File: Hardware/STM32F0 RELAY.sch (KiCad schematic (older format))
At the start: 22 parts, among them Q2 Q_NMOS_GSD, U10 STM32F030RCT6, Y3 32.768kHz, Y4 8MHz

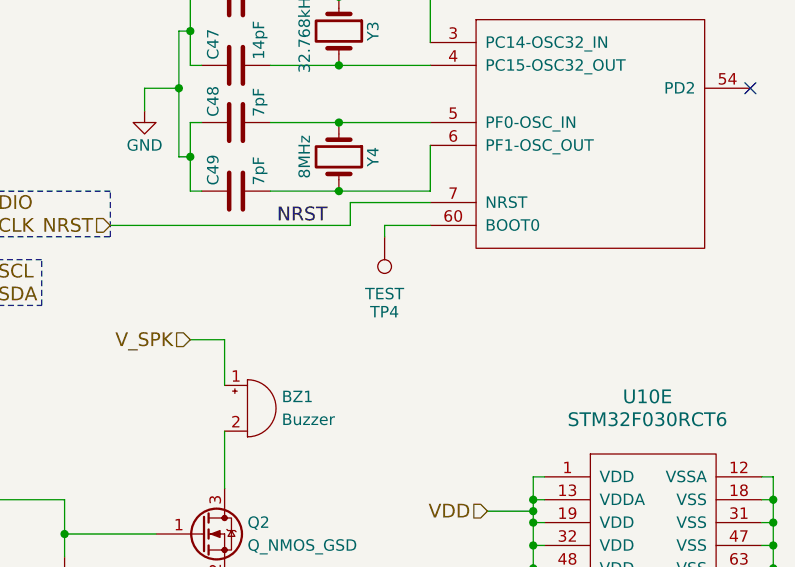
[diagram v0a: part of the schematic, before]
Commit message: Bug fixes, added Isense, changed conn to JST-GH
Added boot0 pull-down resistors. Changed ext_batt to current sense line. Changed spox conn to JST-GH, this will dramatically reduce the required size of the board.
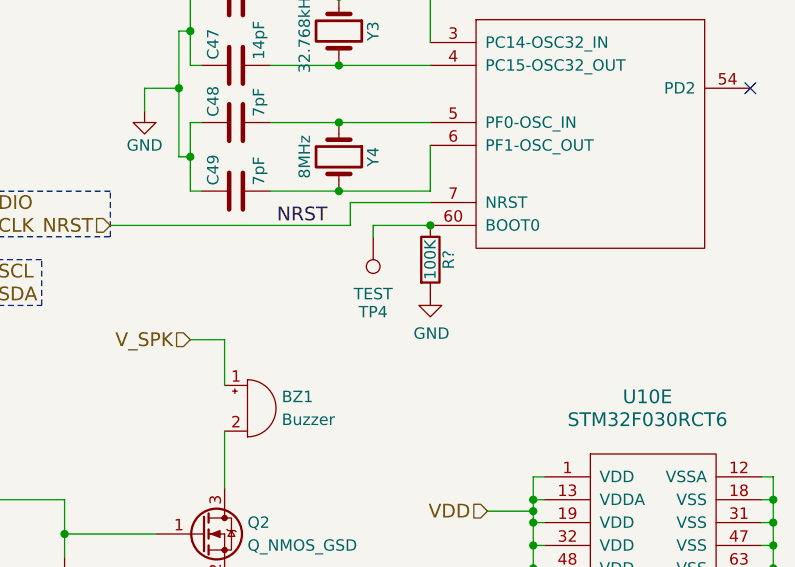
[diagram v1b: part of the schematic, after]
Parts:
- added R?: 100K, Resistors_SMD:R_0603_HandSoldering, symbol Device:R
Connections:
- net GND: now also R?.2
- net at TP4.1, U10.60 (BOOT0): now also R?.1
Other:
- moved on the sheet: TP4
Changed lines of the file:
@@
 L Connector:TestPoint TP4
 U 1 1 596A3495
-P 7200 3200
-F 0 "TP4" H 7200 3500 50  0000 C BNN
-F 1 "TEST" H 7200 3450 50  0000 C CNN
-F 2 "Measurement_Points:Measurement_Point_Round-SMD-Pad_Small" H 7200 3200 50  0001 C CNN
-F 3 "" H 7200 3200 50  0001 C CNN
-	1    7200 3200
+P 7150 3200
+F 0 "TP4" H 7150 3500 50  0000 C BNN
+F 1 "TEST" H 7150 3450 50  0000 C CNN
+F 2 "Measurement_Points:Measurement_Point_Round-SMD-Pad_Small" H 7150 3200 50  0001 C CNN
+F 3 "" H 7150 3200 50  0001 C CNN
+	1    7150 3200
 	-1   0    0    1
 $EndComp
 Wire Wire Line
-	7200 3200 7200 3150
-Wire Wire Line
-	7200 3150 7400 3150
+	7150 3200 7150 3150
+Wire Wire Line
+	7150 3150 7400 3150
 NoConn ~ 3900 5400
 NoConn ~ 3900 5300
@@
 Wire Notes Line
 	3050 2900 3050 2700
+$Comp
+L Device:R R?
+U 1 1 5CBCEAA5
+P 7400 3300
+F 0 "R?" V 7480 3300 50  0000 C CNN
+F 1 "100K" V 7400 3300 50  0000 C CNN
+F 2 "Resistors_SMD:R_0603_HandSoldering" V 7330 3300 50  0001 C CNN
+F 3 "http://www.yageo.com/documents/recent/PYu-RC_Group_51_RoHS_L_10.pdf" H 7400 3300 50  0001 C CNN
+F 4 "RESS-008" V 7400 3300 60  0001 C CNN "part_num"
+	1    7400 3300
+	1    0    0    -1
+$EndComp
+Connection ~ 7400 3150
 Wire Bus Line
 	1400 3700 1400 5350
+$Comp
+L power:GND #PWR?
+U 1 1 5CBD6D08
+P 7400 3450
+F 0 "#PWR?" H 7400 3200 50  0001 C CNN
+F 1 "GND" H 7405 3277 50  0000 C CNN
+F 2 "" H 7400 3450 50  0001 C CNN
+F 3 "" H 7400 3450 50  0001 C CNN
+	1    7400 3450
+	1    0    0    -1
+$EndComp
 $EndSCHEMATC

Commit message: Added protection diode to USB
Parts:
- R?: value 100K -> 10K; part_num RESS-008 -> RESS-005
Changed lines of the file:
@@
 P 7400 3300
 F 0 "R?" V 7480 3300 50  0000 C CNN
-F 1 "100K" V 7400 3300 50  0000 C CNN
+F 1 "10K" V 7400 3300 50  0000 C CNN
 F 2 "Resistors_SMD:R_0603_HandSoldering" V 7330 3300 50  0001 C CNN
 F 3 "http://www.yageo.com/documents/recent/PYu-RC_Group_51_RoHS_L_10.pdf" H 7400 3300 50  0001 C CNN
-F 4 "RESS-008" V 7400 3300 60  0001 C CNN "part_num"
+F 4 "RESS-005" V 7400 3300 60  0001 C CNN "part_num"
 	1    7400 3300
 	1    0    0    -1
 $EndComp
 Connection ~ 7400 3150
-Wire Bus Line
-	1400 3700 1400 5350
 $Comp
 L power:GND #PWR?
@@
 	1    0    0    -1
 $EndComp
+Wire Bus Line
+	1400 3700 1400 5350
 $EndSCHEMATC

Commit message: Removed F0 SPI, gave Baro its own I2C line, changed IMU to SPI1
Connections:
- net MISO: no longer names the net of U10.56 (PB4)
- net MOSI: no longer names the net of U10.57 (PB5)
- net NSS: no longer names the net of U10.50 (PA15)
- net SCLK: no longer names the net of U10.55 (PB3)
- no-connect marks 17 -> 21
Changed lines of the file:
@@
 EESchema Schematic File Version 4
-LIBS:ZeroPilot-cache
 EELAYER 26 0
 EELAYER END
@@
 Wire Wire Line
 	4950 5300 6150 5300
-Text HLabel 3200 4350 0    60   Input ~ 0
-MOSI
-Text HLabel 3200 4250 0    60   Input ~ 0
-MISO
-Text HLabel 4950 3250 2    60   Input ~ 0
-NSS
-Wire Wire Line
-	4950 3250 4850 3250
-Wire Wire Line
-	3900 4250 3200 4250
-Wire Wire Line
-	3200 4350 3900 4350
-Text HLabel 3200 4150 0    60   Input ~ 0
-SCLK
-Wire Wire Line
-	3200 4150 3900 4150
 $Comp
 L power:GND #PWR034
@@
 	1    0    0    -1
 $EndComp
+NoConn ~ 3900 4350
+NoConn ~ 3900 4250
+NoConn ~ 3900 4150
+NoConn ~ 4850 3250
 Wire Bus Line
 	1400 3700 1400 5350

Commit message: Generated netlist and board outline
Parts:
- gave numbers to parts that had none: 1
- renumbered D9 to D10, D7 to D8, D8 to D9, R20 to R23, R21 to R24, R22 to R25, R23 to R26, TP4 to TP7
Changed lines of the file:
@@
 Connection ~ 7200 5300
 $Comp
-L power:GND #PWR029
+L power:GND #PWR036
 U 1 1 59199AA1
 P 7450 5300
-F 0 "#PWR029" H 7450 5050 50  0001 C CNN
+F 0 "#PWR036" H 7450 5050 50  0001 C CNN
 F 1 "GND" H 7450 5150 50  0000 C CNN
 F 2 "" H 7450 5300 50  0001 C CNN
@@
 Connection ~ 6350 2300
 $Comp
-L power:GND #PWR030
+L power:GND #PWR032
 U 1 1 5919B18A
 P 6150 2650
-F 0 "#PWR030" H 6150 2400 50  0001 C CNN
+F 0 "#PWR032" H 6150 2400 50  0001 C CNN
 F 1 "GND" H 6150 2500 50  0000 C CNN
 F 2 "" H 6150 2650 50  0001 C CNN
@@
 	2500 4400 3200 4400
 $Comp
-L Device:LED D8
+L Device:LED D9
 U 1 1 59531E55
 P 5800 5750
-F 0 "D8" H 5800 5850 50  0000 C CNN
+F 0 "D9" H 5800 5850 50  0000 C CNN
 F 1 "LED" H 5800 5650 50  0000 C CNN
 F 2 "LEDs:LED_0603" H 5800 5750 50  0001 C CNN
@@
 $EndComp
 $Comp
-L Device:R R22
+L Device:R R25
 U 1 1 59531EA2
 P 5800 6150
-F 0 "R22" V 5880 6150 50  0000 C CNN
+F 0 "R25" V 5880 6150 50  0000 C CNN
 F 1 "100" V 5800 6150 50  0000 C CNN
 F 2 "Resistors_SMD:R_0603_HandSoldering" V 5730 6150 50  0001 C CNN
@@
 VDD
 $Comp
-L Connector:TestPoint TP4
+L Connector:TestPoint TP7
 U 1 1 596A3495
 P 7150 3200
-F 0 "TP4" H 7150 3500 50  0000 C BNN
+F 0 "TP7" H 7150 3500 50  0000 C BNN
 F 1 "TEST" H 7150 3450 50  0000 C CNN
 F 2 "Measurement_Points:Measurement_Point_Round-SMD-Pad_Small" H 7150 3200 50  0001 C CNN
@@
 NoConn ~ 4900 4250
 $Comp
-L Device:LED D7
+L Device:LED D8
 U 1 1 592CEFDB
 P 5450 5750
-F 0 "D7" H 5450 5850 50  0000 C CNN
+F 0 "D8" H 5450 5850 50  0000 C CNN
 F 1 "LED" H 5450 5650 50  0000 C CNN
 F 2 "LEDs:LED_0603" H 5450 5750 50  0001 C CNN
@@
 $EndComp
 $Comp
-L Device:R R20
+L Device:R R23
 U 1 1 592CEFE3
 P 5450 6150
-F 0 "R20" V 5530 6150 50  0000 C CNN
+F 0 "R23" V 5530 6150 50  0000 C CNN
 F 1 "100" V 5450 6150 50  0000 C CNN
 F 2 "Resistors_SMD:R_0603_HandSoldering" V 5380 6150 50  0001 C CNN
@@
 $EndComp
 $Comp
-L power:GND #PWR032
+L power:GND #PWR029
 U 1 1 592CEFEA
 P 5450 6400
-F 0 "#PWR032" H 5450 6150 50  0001 C CNN
+F 0 "#PWR029" H 5450 6150 50  0001 C CNN
 F 1 "GND" H 5450 6250 50  0000 C CNN
 F 2 "" H 5450 6400 50  0001 C CNN
@@
 	5450 6000 5450 5900
 $Comp
-L Device:LED D9
+L Device:LED D10
 U 1 1 592CF150
 P 6150 5750
-F 0 "D9" H 6150 5850 50  0000 C CNN
+F 0 "D10" H 6150 5850 50  0000 C CNN
 F 1 "LED" H 6150 5650 50  0000 C CNN
 F 2 "LEDs:LED_0603" H 6150 5750 50  0001 C CNN
@@
 $EndComp
 $Comp
-L Device:R R23
+L Device:R R26
 U 1 1 592CF158
 P 6150 6150
-F 0 "R23" V 6230 6150 50  0000 C CNN
+F 0 "R26" V 6230 6150 50  0000 C CNN
 F 1 "100" V 6150 6150 50  0000 C CNN
 F 2 "Resistors_SMD:R_0603_HandSoldering" V 6080 6150 50  0001 C CNN
@@
 	4950 5300 6150 5300
 $Comp
-L power:GND #PWR034
+L power:GND #PWR030
 U 1 1 594F28B6
 P 5800 5000
-F 0 "#PWR034" H 5800 4750 50  0001 C CNN
+F 0 "#PWR030" H 5800 4750 50  0001 C CNN
 F 1 "GND" H 5800 4850 50  0000 C CNN
 F 2 "" H 5800 5000 50  0001 C CNN
@@
 	5800 4350 4900 4350
 $Comp
-L Device:R R21
+L Device:R R24
 U 1 1 599C8783
 P 5800 4750
-F 0 "R21" V 5880 4750 50  0000 C CNN
+F 0 "R24" V 5880 4750 50  0000 C CNN
 F 1 "100K" V 5800 4750 50  0000 C CNN
 F 2 "Resistors_SMD:R_0603_HandSoldering" V 5730 4750 50  0001 C CNN
@@
 Connection ~ 5800 4500
 $Comp
-L power:GND #PWR035
+L power:GND #PWR034
 U 1 1 599C9676
 P 6500 4800
-F 0 "#PWR035" H 6500 4550 50  0001 C CNN
+F 0 "#PWR034" H 6500 4550 50  0001 C CNN
 F 1 "GND" H 6500 4650 50  0000 C CNN
 F 2 "" H 6500 4800 50  0001 C CNN
@@
 	3050 2900 3050 2700
 $Comp
-L Device:R R?
+L Device:R R27
 U 1 1 5CBCEAA5
 P 7400 3300
-F 0 "R?" V 7480 3300 50  0000 C CNN
+F 0 "R27" V 7480 3300 50  0000 C CNN
 F 1 "10K" V 7400 3300 50  0000 C CNN
 F 2 "Resistors_SMD:R_0603_HandSoldering" V 7330 3300 50  0001 C CNN
@@
 Connection ~ 7400 3150
 $Comp
-L power:GND #PWR?
+L power:GND #PWR035
 U 1 1 5CBD6D08
 P 7400 3450
-F 0 "#PWR?" H 7400 3200 50  0001 C CNN
+F 0 "#PWR035" H 7400 3200 50  0001 C CNN
 F 1 "GND" H 7405 3277 50  0000 C CNN
 F 2 "" H 7400 3450 50  0001 C CNN

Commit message: Updated Footprints
Updated the footprints to 5.1, added 3D models to all components.
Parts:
- C46, C47, C48, C49, C50, C51, C52, C53, C54: footprint Capacitors_SMD:C_0603_HandSoldering -> Capacitor_SMD:C_0603_1608Metric_Pad1.05x0.95mm_HandSolder
- D10, D8, D9: footprint LEDs:LED_0603 -> LED_SMD:LED_0603_1608Metric_Pad1.05x0.95mm_HandSolder
- Q2: footprint TO_SOT_Packages_SMD:TSOT-23 -> Package_TO_SOT_SMD:TSOT-23
- R23, R24, R25, R26, R27: footprint Resistors_SMD:R_0603_HandSoldering -> Resistor_SMD:R_0603_1608Metric_Pad1.05x0.95mm_HandSolder
- TP7: footprint Measurement_Points:Measurement_Point_Round-SMD-Pad_Small -> TestPoint:TestPoint_Pad_D1.5mm
- U10: footprint Housings_QFP:LQFP-64_10x10mm_Pitch0.5mm -> Package_QFP:LQFP-64_10x10mm_P0.5mm
- Y3: footprint Crystals:Crystal_SMD_MicroCrystal_CC7V-T1A-2pin_3.2x1.5mm_HandSoldering -> Crystal:Crystal_SMD_MicroCrystal_CC7V-T1A-2Pin_3.2x1.5mm
- Y4: footprint Crystals:Crystal_SMD_5032-2pin_5.0x3.2mm_HandSoldering -> Crystal:Crystal_SMD_5032-2Pin_5.0x3.2mm_HandSoldering

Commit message: HW Bootcamp for Zeropilot R1
Changed the board to R1.
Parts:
- renumbered C46 to C43, C47 to C44, C48 to C45, C49 to C46, C50 to C47, C51 to C48, C52 to C49, C53 to C50, C54 to C51, R23 to R21, R24 to R22, R25 to R23, R26 to R24, R27 to R25, U10 to U5
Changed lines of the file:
@@
 EESchema Schematic File Version 4
-LIBS:ZeroPilot-cache
 EELAYER 29 0
 EELAYER END
@@
 Connection ~ 8900 4650
 $Comp
-L Device:C C51
+L Device:C C48
 U 1 1 5919967A
 P 7200 5050
-F 0 "C51" H 7225 5150 50  0000 L CNN
+F 0 "C48" H 7225 5150 50  0000 L CNN
 F 1 "100nF" H 7225 4950 50  0000 L CNN
 F 2 "Capacitor_SMD:C_0603_1608Metric_Pad1.05x0.95mm_HandSolder" H 7238 4900 50  0001 C CNN
@@
 $EndComp
 $Comp
-L Device:C C52
+L Device:C C49
 U 1 1 591996BB
 P 7450 5050
-F 0 "C52" H 7475 5150 50  0000 L CNN
+F 0 "C49" H 7475 5150 50  0000 L CNN
 F 1 "4.7uF" H 7475 4950 50  0000 L CNN
 F 2 "Capacitor_SMD:C_0603_1608Metric_Pad1.05x0.95mm_HandSolder" H 7488 4900 50  0001 C CNN
@@
 $EndComp
 $Comp
-L Device:C C53
+L Device:C C50
 U 1 1 591996E8
 P 7700 5050
-F 0 "C53" H 7725 5150 50  0000 L CNN
+F 0 "C50" H 7725 5150 50  0000 L CNN
 F 1 "10nF" H 7725 4950 50  0000 L CNN
 F 2 "Capacitor_SMD:C_0603_1608Metric_Pad1.05x0.95mm_HandSolder" H 7738 4900 50  0001 C CNN
@@
 $EndComp
 $Comp
-L Device:C C50
+L Device:C C47
 U 1 1 5919971A
 P 6950 5050
-F 0 "C50" H 6975 5150 50  0000 L CNN
+F 0 "C47" H 6975 5150 50  0000 L CNN
 F 1 "100nF" H 6975 4950 50  0000 L CNN
 F 2 "Capacitor_SMD:C_0603_1608Metric_Pad1.05x0.95mm_HandSolder" H 6988 4900 50  0001 C CNN
@@
 $EndComp
 $Comp
-L Device:C C54
+L Device:C C51
 U 1 1 5919974F
 P 7950 5050
-F 0 "C54" H 7975 5150 50  0000 L CNN
+F 0 "C51" H 7975 5150 50  0000 L CNN
 F 1 "1uF" H 7975 4950 50  0000 L CNN
 F 2 "Capacitor_SMD:C_0603_1608Metric_Pad1.05x0.95mm_HandSolder" H 7988 4900 50  0001 C CNN
@@
 Connection ~ 7200 5300
 $Comp
-L power:GND #PWR036
+L power:GND #PWR031
 U 1 1 59199AA1
 P 7450 5300
-F 0 "#PWR036" H 7450 5050 50  0001 C CNN
+F 0 "#PWR031" H 7450 5050 50  0001 C CNN
 F 1 "GND" H 7450 5150 50  0000 C CNN
 F 2 "" H 7450 5300 50  0001 C CNN
@@
 	7400 2150 7400 2350
 $Comp
-L Device:C C48
+L Device:C C45
 U 1 1 5919AAC2
 P 6550 2700
-F 0 "C48" H 6575 2800 50  0000 L CNN
+F 0 "C45" H 6575 2800 50  0000 L CNN
 F 1 "7pF" H 6575 2600 50  0000 L CNN
 F 2 "Capacitor_SMD:C_0603_1608Metric_Pad1.05x0.95mm_HandSolder" H 6588 2550 50  0001 C CNN
@@
 $EndComp
 $Comp
-L Device:C C49
+L Device:C C46
 U 1 1 5919AB20
 P 6550 3000
-F 0 "C49" H 6575 3100 50  0000 L CNN
+F 0 "C46" H 6575 3100 50  0000 L CNN
 F 1 "7pF" H 6575 2900 50  0000 L CNN
 F 2 "Capacitor_SMD:C_0603_1608Metric_Pad1.05x0.95mm_HandSolder" H 6588 2850 50  0001 C CNN
@@
 $EndComp
 $Comp
-L Device:C C47
+L Device:C C44
 U 1 1 5919ABF0
 P 6550 2450
-F 0 "C47" H 6575 2550 50  0000 L CNN
+F 0 "C44" H 6575 2550 50  0000 L CNN
 F 1 "14pF" H 6575 2350 50  0000 L CNN
 F 2 "Capacitor_SMD:C_0603_1608Metric_Pad1.05x0.95mm_HandSolder" H 6588 2300 50  0001 C CNN
@@
 $EndComp
 $Comp
-L Device:C C46
+L Device:C C43
 U 1 1 5919AC3B
 P 6550 2150
-F 0 "C46" H 6575 2250 50  0000 L CNN
+F 0 "C43" H 6575 2250 50  0000 L CNN
 F 1 "14pF" H 6575 2050 50  0000 L CNN
 F 2 "Capacitor_SMD:C_0603_1608Metric_Pad1.05x0.95mm_HandSolder" H 6588 2000 50  0001 C CNN
@@
 Connection ~ 6350 2300
 $Comp
-L power:GND #PWR032
+L power:GND #PWR027
 U 1 1 5919B18A
 P 6150 2650
-F 0 "#PWR032" H 6150 2400 50  0001 C CNN
+F 0 "#PWR027" H 6150 2400 50  0001 C CNN
 F 1 "GND" H 6150 2500 50  0000 C CNN
 F 2 "" H 6150 2650 50  0001 C CNN
@@
 $EndComp
 $Comp
-L Device:R R25
+L Device:R R23
 U 1 1 59531EA2
 P 5800 6150
-F 0 "R25" V 5880 6150 50  0000 C CNN
+F 0 "R23" V 5880 6150 50  0000 C CNN
 F 1 "100" V 5800 6150 50  0000 C CNN
 F 2 "Resistor_SMD:R_0603_1608Metric_Pad1.05x0.95mm_HandSolder" V 5730 6150 50  0001 C CNN
@@
 $EndComp
 $Comp
-L power:GND #PWR031
+L power:GND #PWR026
 U 1 1 59531EED
 P 5800 6400
-F 0 "#PWR031" H 5800 6150 50  0001 C CNN
+F 0 "#PWR026" H 5800 6150 50  0001 C CNN
 F 1 "GND" H 5800 6250 50  0000 C CNN
 F 2 "" H 5800 6400 50  0001 C CNN
@@
 VDD
 $Comp
-L Connector:TestPoint TP7
+L Connector:TestPoint TP?
 U 1 1 596A3495
 P 7150 3200
-AR Path="/596A3495" Ref="TP7"  Part="1"
+AR Path="/596A3495" Ref="TP?"  Part="1"
 AR Path="/5919369D/596A3495" Ref="TP7"  Part="1"
 F 0 "TP7" H 7150 3500 50  0000 C BNN
@@
 $EndComp
 $Comp
-L Device:R R23
+L Device:R R21
 U 1 1 592CEFE3
 P 5450 6150
-F 0 "R23" V 5530 6150 50  0000 C CNN
+F 0 "R21" V 5530 6150 50  0000 C CNN
 F 1 "100" V 5450 6150 50  0000 C CNN
 F 2 "Resistor_SMD:R_0603_1608Metric_Pad1.05x0.95mm_HandSolder" V 5380 6150 50  0001 C CNN
@@
 $EndComp
 $Comp
-L power:GND #PWR029
+L power:GND #PWR024
 U 1 1 592CEFEA
 P 5450 6400
-F 0 "#PWR029" H 5450 6150 50  0001 C CNN
+F 0 "#PWR024" H 5450 6150 50  0001 C CNN
 F 1 "GND" H 5450 6250 50  0000 C CNN
 F 2 "" H 5450 6400 50  0001 C CNN
@@
 $EndComp
 $Comp
-L Device:R R26
+L Device:R R24
 U 1 1 592CF158
 P 6150 6150
-F 0 "R26" V 6230 6150 50  0000 C CNN
+F 0 "R24" V 6230 6150 50  0000 C CNN
 F 1 "100" V 6150 6150 50  0000 C CNN
 F 2 "Resistor_SMD:R_0603_1608Metric_Pad1.05x0.95mm_HandSolder" V 6080 6150 50  0001 C CNN
@@
 $EndComp
 $Comp
-L power:GND #PWR033
+L power:GND #PWR028
 U 1 1 592CF15F
 P 6150 6400
-F 0 "#PWR033" H 6150 6150 50  0001 C CNN
+F 0 "#PWR028" H 6150 6150 50  0001 C CNN
 F 1 "GND" H 6150 6250 50  0000 C CNN
 F 2 "" H 6150 6400 50  0001 C CNN
@@
 	4950 5300 6150 5300
 $Comp
-L power:GND #PWR030
+L power:GND #PWR025
 U 1 1 594F28B6
 P 5800 5000
-F 0 "#PWR030" H 5800 4750 50  0001 C CNN
+F 0 "#PWR025" H 5800 4750 50  0001 C CNN
 F 1 "GND" H 5800 4850 50  0000 C CNN
 F 2 "" H 5800 5000 50  0001 C CNN
@@
 $EndComp
 $Comp
-L WARG:STM32F030RCT6 U10
+L WARG:STM32F030RCT6 U5
 U 1 1 599C1943
 P 4400 3200
-F 0 "U10" H 4400 4200 60  0000 C CNN
+F 0 "U5" H 4400 4200 60  0000 C CNN
 F 1 "STM32F030RCT6" H 4400 4100 60  0000 C CNN
 F 2 "Package_QFP:LQFP-64_10x10mm_P0.5mm" H 4150 3700 60  0001 C CNN
@@
 $EndComp
 $Comp
-L WARG:STM32F030RCT6 U10
+L WARG:STM32F030RCT6 U5
 U 2 1 599C19BB
 P 4400 4600
-F 0 "U10" H 4400 5600 60  0000 C CNN
+F 0 "U5" H 4400 5600 60  0000 C CNN
 F 1 "STM32F030RCT6" H 4400 5500 60  0000 C CNN
 F 2 "Package_QFP:LQFP-64_10x10mm_P0.5mm" H 4150 5100 60  0001 C CNN
@@
 $EndComp
 $Comp
-L WARG:STM32F030RCT6 U10
+L WARG:STM32F030RCT6 U5
 U 3 1 599C1A21
 P 4400 5850
-F 0 "U10" H 4400 6850 60  0000 C CNN
+F 0 "U5" H 4400 6850 60  0000 C CNN
 F 1 "STM32F030RCT6" H 4400 6750 60  0000 C CNN
 F 2 "Package_QFP:LQFP-64_10x10mm_P0.5mm" H 4150 6350 60  0001 C CNN
@@
 $EndComp
 $Comp
-L WARG:STM32F030RCT6 U10
+L WARG:STM32F030RCT6 U5
 U 4 1 599C1A7B
 P 8000 3000
-F 0 "U10" H 8000 4000 60  0000 C CNN
+F 0 "U5" H 8000 4000 60  0000 C CNN
 F 1 "STM32F030RCT6" H 8000 3900 60  0000 C CNN
 F 2 "Package_QFP:LQFP-64_10x10mm_P0.5mm" H 7750 3500 60  0001 C CNN
@@
 $EndComp
 $Comp
-L WARG:STM32F030RCT6 U10
+L WARG:STM32F030RCT6 U5
 U 5 1 599C1AE4
 P 8350 4900
-F 0 "U10" H 8350 5900 60  0000 C CNN
+F 0 "U5" H 8350 5900 60  0000 C CNN
 F 1 "STM32F030RCT6" H 8350 5800 60  0000 C CNN
 F 2 "Package_QFP:LQFP-64_10x10mm_P0.5mm" H 8100 5400 60  0001 C CNN
@@
 	5800 4350 4900 4350
 $Comp
-L Device:R R24
+L Device:R R22
 U 1 1 599C8783
 P 5800 4750
-F 0 "R24" V 5880 4750 50  0000 C CNN
+F 0 "R22" V 5880 4750 50  0000 C CNN
 F 1 "100K" V 5800 4750 50  0000 C CNN
 F 2 "Resistor_SMD:R_0603_1608Metric_Pad1.05x0.95mm_HandSolder" V 5730 4750 50  0001 C CNN
@@
 Connection ~ 5800 4500
 $Comp
-L power:GND #PWR034
+L power:GND #PWR029
 U 1 1 599C9676
 P 6500 4800
-F 0 "#PWR034" H 6500 4550 50  0001 C CNN
+F 0 "#PWR029" H 6500 4550 50  0001 C CNN
 F 1 "GND" H 6500 4650 50  0000 C CNN
 F 2 "" H 6500 4800 50  0001 C CNN
@@
 	3050 2900 3050 2700
 $Comp
-L Device:R R27
+L Device:R R25
 U 1 1 5CBCEAA5
 P 7400 3300
-F 0 "R27" V 7480 3300 50  0000 C CNN
+F 0 "R25" V 7480 3300 50  0000 C CNN
 F 1 "10K" V 7400 3300 50  0000 C CNN
 F 2 "Resistor_SMD:R_0603_1608Metric_Pad1.05x0.95mm_HandSolder" V 7330 3300 50  0001 C CNN
@@
 Connection ~ 7400 3150
 $Comp
-L power:GND #PWR035
+L power:GND #PWR030
 U 1 1 5CBD6D08
 P 7400 3450
-F 0 "#PWR035" H 7400 3200 50  0001 C CNN
+F 0 "#PWR030" H 7400 3200 50  0001 C CNN
 F 1 "GND" H 7405 3277 50  0000 C CNN
 F 2 "" H 7400 3450 50  0001 C CNN
